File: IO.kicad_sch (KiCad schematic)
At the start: 0 parts

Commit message: First draft of USB and power module Plus some display started
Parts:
- added C1: 4.7uF, PCM_JLCPCB:C_0402, symbol PCM_JLCPCB-Capacitors:0402,4.7uF
- added C2: 100nF, PCM_JLCPCB:C_0603, symbol PCM_JLCPCB-Capacitors:0603,100nF
- added C3: 10uF, PCM_JLCPCB:C_0603, symbol PCM_JLCPCB-Capacitors:0603,10uF
- added IC1: TPS63001DRCR, TPS74901DRCR, symbol E-paper-library:TPS63001DRCR
- added J1: Connector, USB-TYPE-C-16P, PCM_JLCPCB:TYPE-C-SMD_HX-TYPE-C-16PIN, symbol PCM_JLCPCB-Extended:Connector, USB-TYPE-C-16P
- added L1: 2.2uH, symbol Device:L
- added R1, R2: 5.1kΩ, PCM_JLCPCB:R_0603, symbol PCM_JLCPCB-Resistors:0603,5.1kΩ
- added R3: 1MΩ, PCM_JLCPCB:R_0603, symbol PCM_JLCPCB-Resistors:0603,1MΩ
- added R4: 10Ω, PCM_JLCPCB:R_0603, symbol PCM_JLCPCB-Resistors:0603,10Ω
- added SW1: MK-12C02-G020, MK-12C02-G020_GSW, symbol E-paper-library:MK-12C02-G020
- added U1: SRV05-4.TCT, SO6_SOT23-6L, symbol E-paper-library:SRV05-4.TCT
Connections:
- new net: J1.B5 (CC2), R2.1
- new net: C1.1, J1.S1 (SHIELD), R3.1
- new net: J1.A5 (CC1), R1.2
- new net +3.3V: IC1.10 (FB)
- new net 5V_USB: C3.1, IC1.5 (VIN), J1.A9B4 (VBUS), J1.B9A4 (VBUS), R4.1, U1.5
- new net EN: IC1.6 (EN), SW1.3
- new net GNDD: C1.2, C2.2, C3.2, IC1.3 (PGND), IC1.9 (GND), IC1.EP1 (EP), J1.A12B1 (GND), J1.B12A1 (GND), R1.1, R2.2, R3.2, U1.2
- new net L1: IC1.4 (L1), L1.2
- new net L2: IC1.2 (L2), L1.1
- new net PS/SYNC: IC1.7 (PS/SYNC)
- new net USB D+: J1.A6 (D+), J1.B6 (D+), U1.1
- new net USB D-: J1.A7 (D-), J1.B7 (D-), U1.3
- new net VINA: C2.1, IC1.8 (VINA), R4.2, SW1.1
- no-connect marks 0 -> 5
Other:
- note added: "(Connection source)"
- note added: "Decoupling capacitor"
- note added: "ESD protection"
- note added: "Make sure C2 is close to TPS63001 GND!"
- note added: "Peripheral USB mode"
- note added: "Power module"
- note added: "Prevent EMI/ground loop"
- note added: "USB C module"
- note added: "USB Mode selection (audio, etc)"
- note added: "Voltage Regulator ON/OFF Switch"

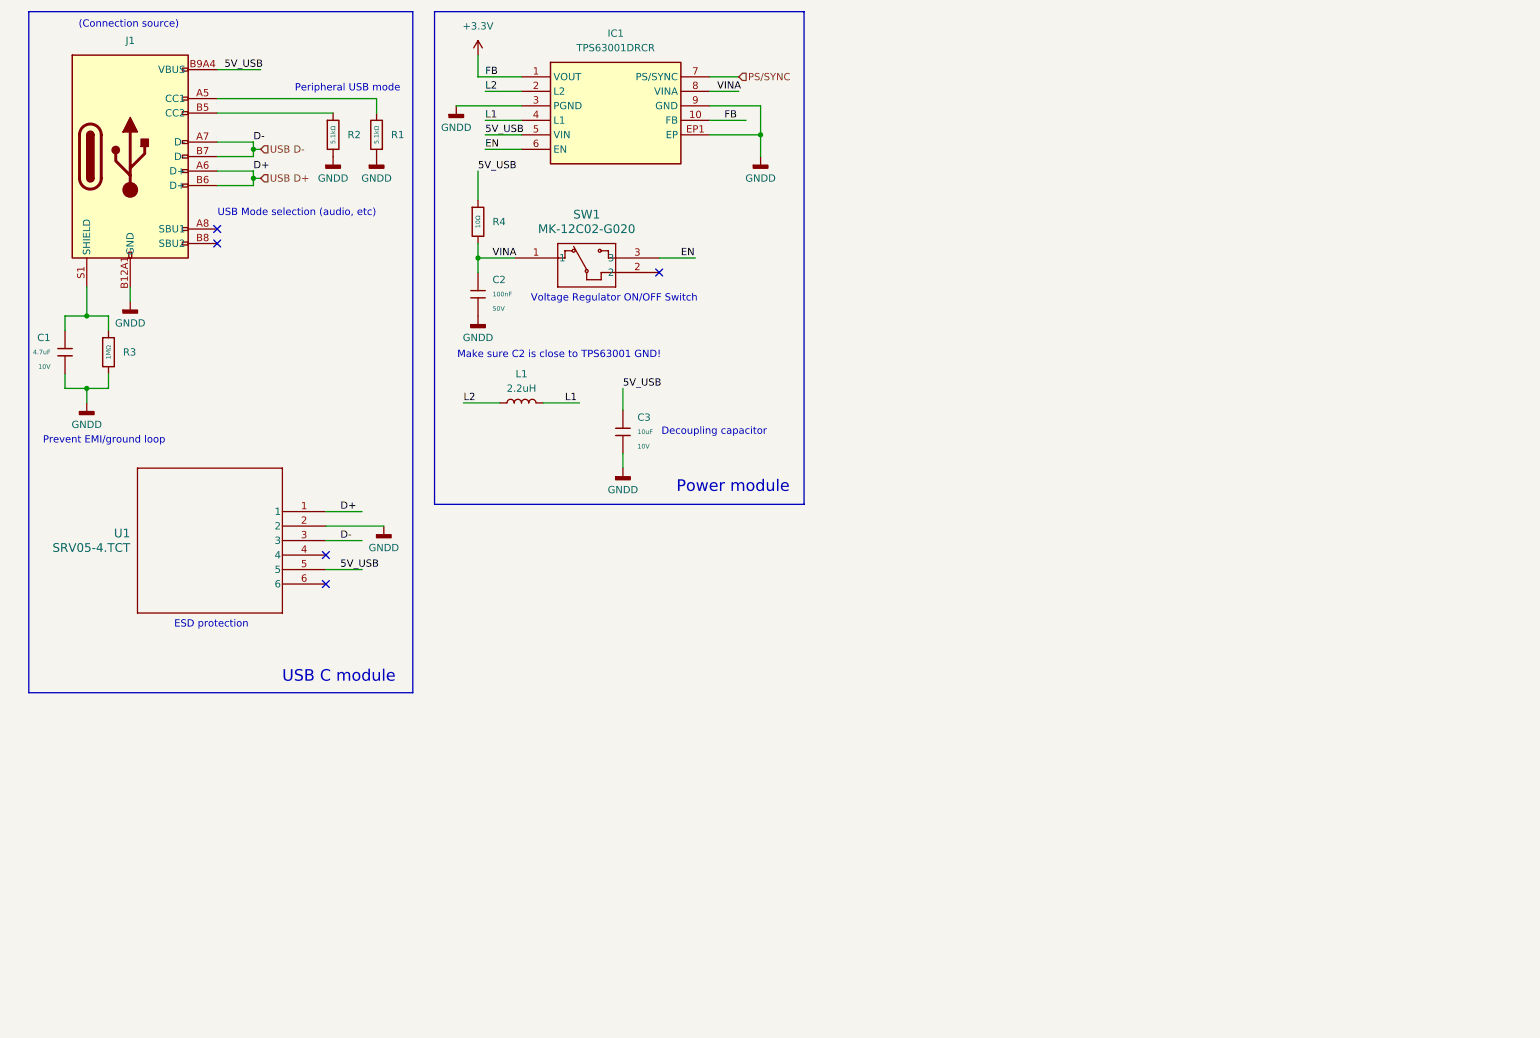
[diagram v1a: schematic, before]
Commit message: Only missing Eframe - Mostly finished MCU - Added Test points to IO - Added LiPo charger - Added Power Source Selection - Added SD card module + SPI connections
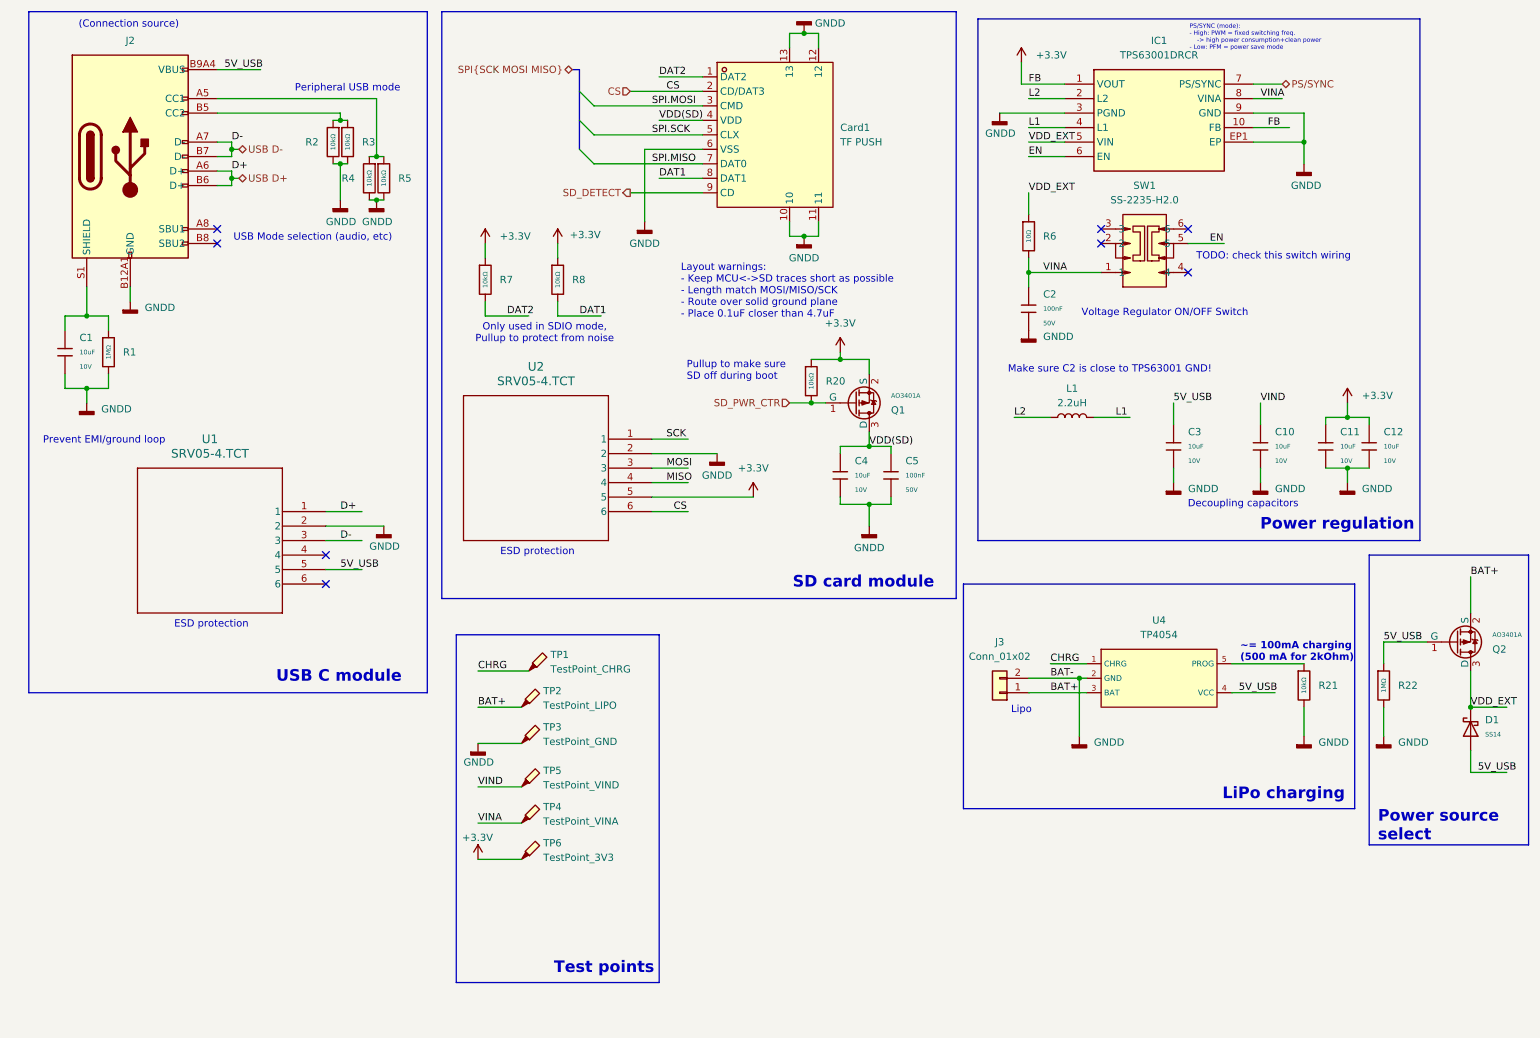
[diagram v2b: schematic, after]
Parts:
- removed C1: 4.7uF, PCM_JLCPCB:C_0402, symbol PCM_JLCPCB-Capacitors:0402,4.7uF
- removed R1, R2: 5.1kΩ, PCM_JLCPCB:R_0603, symbol PCM_JLCPCB-Resistors:0603,5.1kΩ
- removed SW1: MK-12C02-G020, MK-12C02-G020_GSW, symbol E-paper-library:MK-12C02-G020
- added C1, C10, C11, C12, C4: 10uF, PCM_JLCPCB:C_0603, symbol PCM_JLCPCB-Capacitors:0603,10uF
- added C5: 100nF, PCM_JLCPCB:C_0603, symbol PCM_JLCPCB-Capacitors:0603,100nF
- added Card1: TF PUSH, sd_card:TF-SMD_TF-PUSH, symbol E-paper-library:TFPUSH
- added D1: SS14, PCM_JLCPCB:D_SMA, symbol PCM_JLCPCB-Diodes:Schottky,SS14
- added J3: Conn_01x02, symbol Connector_Generic:Conn_01x02
- added Q1, Q2: AO3401A, PCM_JLCPCB:Q_SOT-23, symbol PCM_JLCPCB-Transistors:PMOS,AO3401A
- added R2, R20, R21, R3, R4, R5, R7, R8: 10kΩ, PCM_JLCPCB:R_0402, symbol PCM_JLCPCB-Resistors:0402,10kΩ
- added R22: 1MΩ, PCM_JLCPCB:R_0603, symbol PCM_JLCPCB-Resistors:0603,1MΩ
- added SW1: SS-2235-H2.0, switch:SW-TH_6P-L9.5-W3.5-P2.50_SS-2235-H2.0, symbol E-paper-library:SS-2235-H2.0
- added TP1: TestPoint_CHRG, symbol Connector:TestPoint_Probe
- added TP2: TestPoint_LIPO, symbol Connector:TestPoint_Probe
- added TP3: TestPoint_GND, symbol Connector:TestPoint_Probe
- added TP4: TestPoint_VINA, symbol Connector:TestPoint_Probe
- added TP5: TestPoint_VIND, symbol Connector:TestPoint_Probe
- added TP6: TestPoint_3V3, symbol Connector:TestPoint_Probe
- added U2: SRV05-4.TCT, SO6_SOT23-6L, symbol E-paper-library:SRV05-4.TCT
- added U4: TP4054, PCM_JLCPCB:SOT-23-5_L3.0-W1.7-P0.95-LS2.8-BL, symbol PCM_JLCPCB-Power:Battery, Li-Ion, 0.8A, TP4054
- renumbered J1 to J2, R3 to R1, R4 to R6
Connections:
- net +3.3V: now also C11.1, C12.1, Q1.2 (S), R20.1, R7.1, R8.1, TP6.1, U2.5
- net 5V_USB: now also D1.2, Q2.1 (G), R22.1, U4.4 (VCC); no longer IC1.5 (VIN), R6.1
- net EN: now also SW1.5
- net GNDD: now also C1.2, C10.2, C11.2, C12.2, C4.2, C5.2, Card1.10, Card1.11, Card1.12, Card1.13, Card1.6 (VSS), J3.2 (Pin_2), R2.2, R21.2, R22.2, R3.2, R4.2, R5.2, TP3.1, U2.2, U4.2 (GND)
- net VINA: now also SW1.1, TP4.1
- net at J2.B5 (CC2): now also R2.1, R3.1
- net at J2.S1 (SHIELD), R1.1: now also C1.1
- net at J2.A5 (CC1): now also R4.1, R5.1
- new net: R21.1, U4.5 (PROG)
- new net BAT+: J3.1 (Pin_1), Q2.2 (S), TP2.1, U4.3 (BAT)
- new net CHRG: TP1.1, U4.1 (CHRG)
- new net CS: Card1.2 (CD/DAT3), U2.6
- new net DAT1: Card1.8 (DAT1), R8.2
- new net DAT2: Card1.1 (DAT2), R7.2
- new net MISO: U2.4
- new net MOSI: U2.3
- new net SCK: U2.1
- new net SD_DETECT: Card1.9 (CD)
- new net SD_PWR_CTR: Q1.1 (G), R20.2
- new net SPI.MISO: Card1.7 (DAT0)
- new net SPI.MOSI: Card1.3 (CMD)
- new net SPI.SCK: Card1.5 (CLX)
- new net VDD(SD): C4.1, C5.1, Card1.4 (VDD), Q1.3 (D)
- new net VDD_EXT: D1.1, IC1.5 (VIN), Q2.3 (D), R6.1
- new net VIND: C10.1, TP5.1
- no-connect marks 5 -> 8
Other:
- note added: "Decoupling capacitors"
- note added: "Layout warnings: - Keep MCU<->SD traces short as possible - Length match MOSI/MISO/SCK - Route over solid ground plane - Place 0.1uF closer than 4.7uF"
- note added: "LiPo charging"
- note added: "Lipo"
- note added: "Only used in SDIO mode, Pullup to protect from noise"
- note added: "PS/SYNC (mode): - High: PWM = fixed switching freq. -> high power consumption+clean power - Low: PFM = power save mode"
- note added: "Power regulation"
- note added: "Power source select"
- note added: "Pullup to make sure SD off during boot"
- note added: "SD card module"
- note added: "TODO: check this switch wiring"
- note added: "Test points"
- note added: "~= 100mA charging (500 mA for 2kOhm)"
- note removed: "Decoupling capacitor"
- note removed: "Power module"
- moved on the sheet: C2, C3, IC1, L1, R6

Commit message: Added eframe circuit: - Must replace 10uF caps with higher voltage rated ones - Should double check all the wiring - Assign MCU GPIOs now that all peripherals have their pins assigned
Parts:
- removed L1: 2.2uH, symbol Device:L
- added L2: 2.2uH,50mA, PCM_JLCPCB:L_0805, symbol PCM_JLCPCB-Inductors:2.2uH,50mA
- added TP6: TestPoint_VIND, symbol Connector:TestPoint_Probe
- renumbered C1 to C12, C4 to C13, C5 to C14, C3 to C15, C2 to C16, C10 to C17, C11 to C18, C12 to C19, D1 to D4, J2 to J1, J3 to J2, Q1 to Q3, Q2 to Q4, R3 to R10, R4 to R11, R5 to R12, R7 to R13, R8 to R14, R20 to R15, R6 to R16, R21 to R17, R22 to R18, R1 to R8, R2 to R9, TP2 to TP1, TP3 to TP2, TP4 to TP3, TP6 to TP4, TP1 to TP7, U4 to U3
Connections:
- net EN: now also C16.1, IC1.8 (VINA), R16.2, TP3.1; no longer SW1.5
- net L1: now also L2.2
- net L2: now also L2.1
- net VDD_EXT: now also SW1.3, TP5.1; no longer D4.1, Q4.3 (D)
- net VIND: no longer TP5.1
- net SD_PWR_CTR renamed SD3V3_EN
- removed net VINA: C16.1, IC1.8 (VINA), R16.2, SW1.1, TP3.1
- new net VDD_EXT_OPEN: D4.1, Q4.3 (D), SW1.5, TP6.1
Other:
- note added: "Bulk capacitors"
- note added: "Electrical ON/OFF"
- note removed: "Decoupling capacitors"
- note removed: "TODO: check this switch wiring"
- moved on the sheet: C15, C17, C18, C19, D4, J2, Q4, R17, R18, TP3, TP4, TP5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

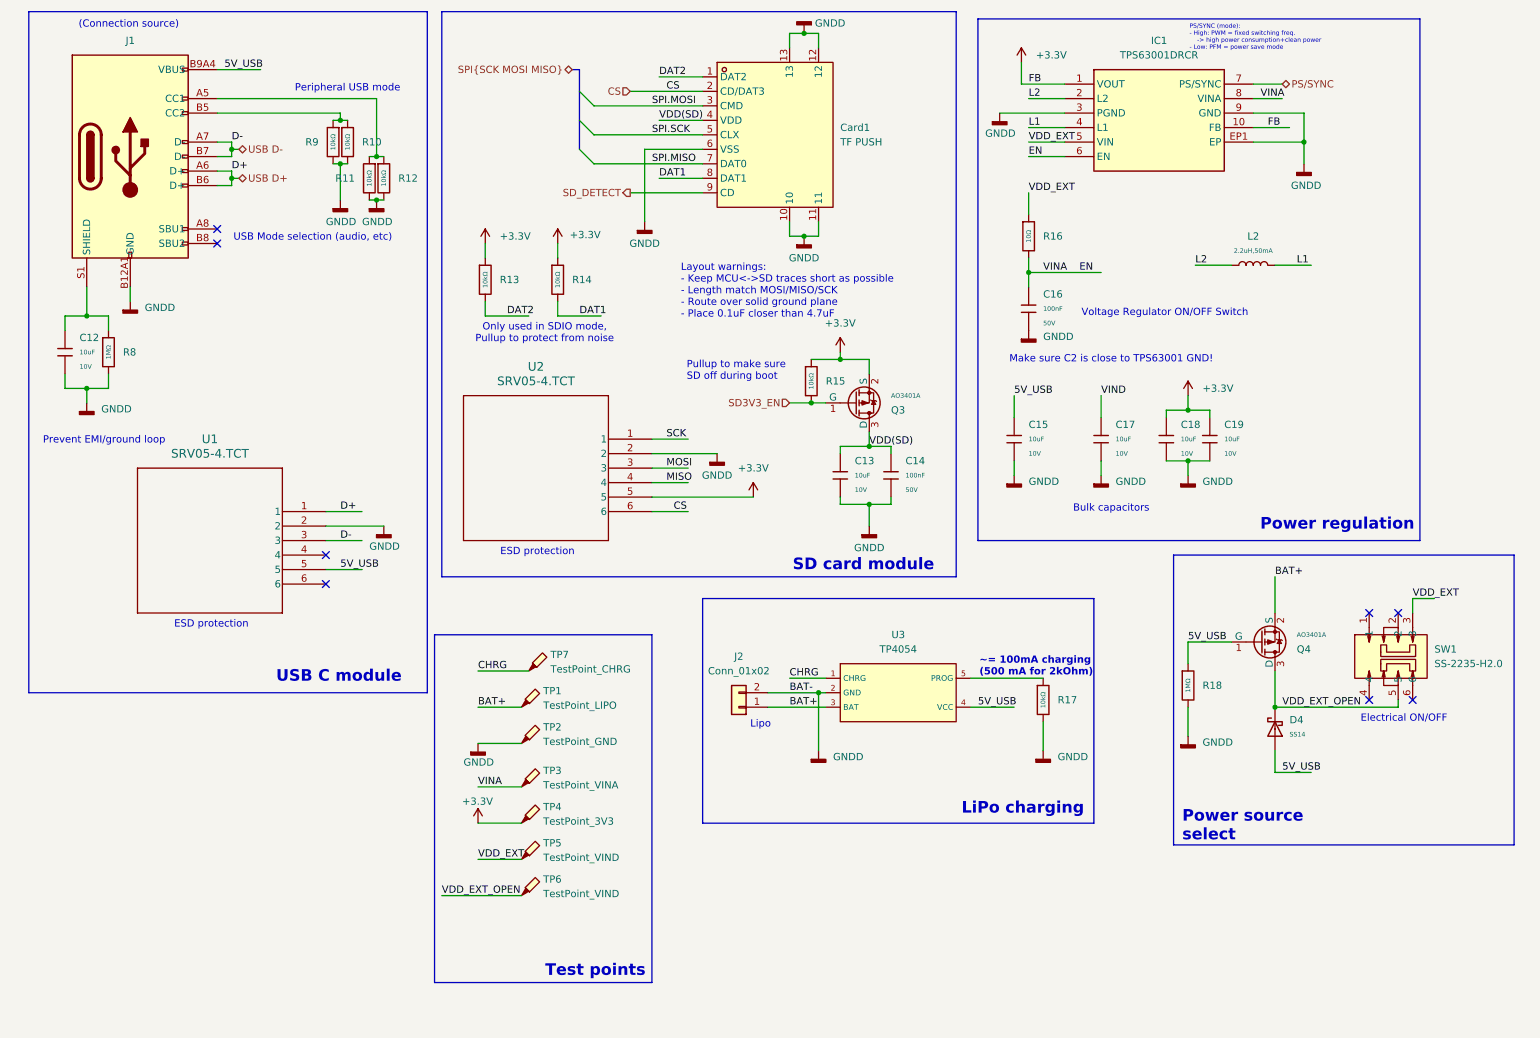
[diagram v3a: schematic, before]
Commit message: Final touches on schematic: Added test points Added LED Fixed symbol footprints
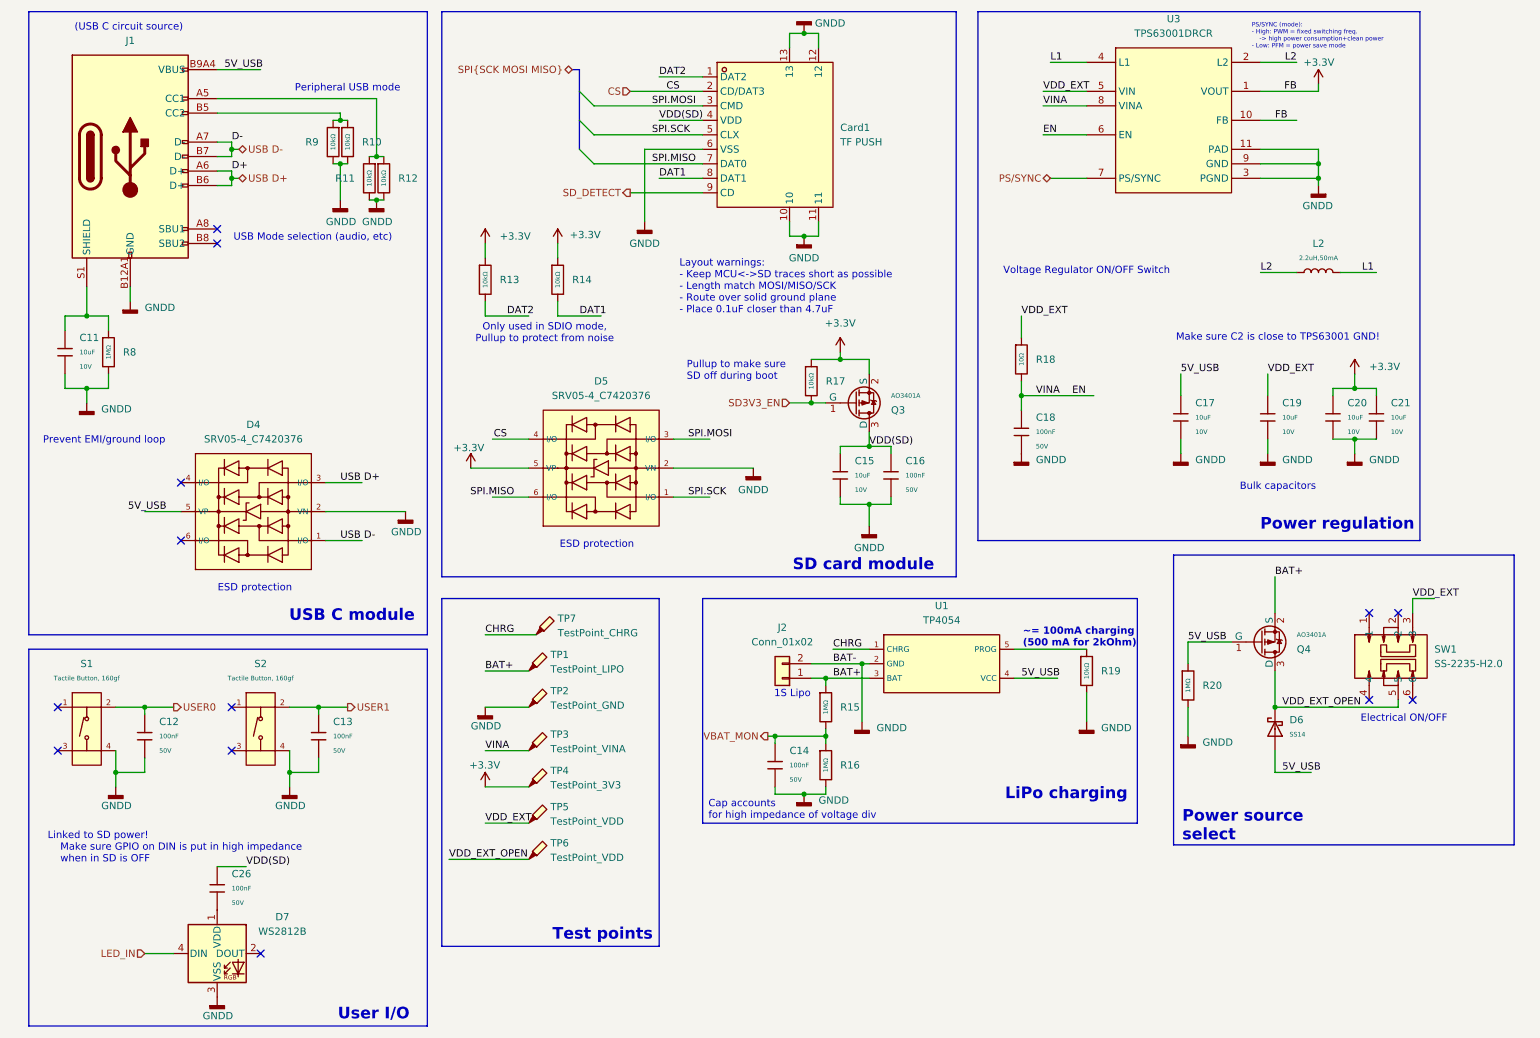
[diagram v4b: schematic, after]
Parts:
- removed IC1: TPS63001DRCR, TPS74901DRCR, symbol E-paper-library:TPS63001DRCR
- removed U1, U2: SRV05-4.TCT, SO6_SOT23-6L, symbol E-paper-library:SRV05-4.TCT
- added C12, C13, C14, C26: 100nF, PCM_JLCPCB:C_0603, symbol PCM_JLCPCB-Capacitors:0603,100nF
- added D4, D5: SRV05-4_C7420376, PCM_JLCPCB:SOT-23-6_L2.9-W1.6-P0.95-LS2.8-BL-1, symbol PCM_JLCPCB-Diode-Packages:Package, SRV05-4_C7420376
- added D7: WS2812B, PCM_JLCPCB:LED_WS2812B_PLCC4_5.0x5.0mm_P3.2mm, symbol PCM_JLCPCB-Extended:LED, WS2812B, 5050
- added R15, R16: 1MΩ, PCM_JLCPCB:R_0603, symbol PCM_JLCPCB-Resistors:0603,1MΩ
- added S1, S2: Tactile Button, 160gf, PCM_JLCPCB:SW-SMD_4P-L5.1-W5.1-P3.70-LS6.5-TL-2, symbol PCM_JLCPCB-Connectors_Buttons:Tactile Button, 160gf, 12V, 50mA, 5.1mm
- added U3: TPS63001DRCR, TPS63001DRCR:VSON-10_L3.0-W3.0-P0.50-TL-EP_TPS62410DRCR, symbol E-paper-library:TPS63001DRCR
- Card1: footprint sd_card:TF-SMD_TF-PUSH -> Libraries:TF-SMD_TF-PUSH
- J2: footprint (none) -> Connector_PinHeader_2.54mm:PinHeader_1x02_P2.54mm_Vertical
- SW1: footprint switch:SW-TH_6P-L9.5-W3.5-P2.50_SS-2235-H2.0 -> Libraries:SW-TH_6P-L9.0-W3.6-P2.50_SS-2235-H2.0
- TP1, TP4: footprint (none) -> TestPoint:TestPoint_Pad_1.5x1.5mm
- TP2, TP3, TP7: footprint (none) -> TestPoint:TestPoint_Pad_D1.5mm
- TP5, TP6: value TestPoint_VIND -> TestPoint_VDD; footprint (none) -> TestPoint:TestPoint_Pad_1.5x1.5mm
- renumbered C12 to C11, C13 to C15, C14 to C16, C15 to C17, C16 to C18, C17 to C19, C18 to C20, C19 to C21, D4 to D6, R15 to R17, R16 to R18, R17 to R19, R18 to R20, U3 to U1
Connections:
- net VIND is gone; now on net VDD_EXT: C19.1
- net +3.3V: now also D5.5 (VP), U3.10 (FB)
- net 5V_USB: now also D4.5 (VP)
- net BAT+: now also R15.1
- net CS: now also D5.4 (I/O)
- net EN: now also U3.6 (EN), U3.8 (VINA)
- net GNDD: now also C12.2, C13.2, C14.2, D4.2 (VN), D5.2 (VN), D7.3 (VSS), R16.2, S1.4 (D), S2.4 (D), U3.11 (PAD), U3.3 (PGND), U3.9 (GND)
- net L1: now also U3.4 (L1)
- net L2: now also U3.2 (L2)
- net PS/SYNC: now also U3.7 (PS/SYNC)
- net SPI.MISO: now also D5.6 (I/O)
- net SPI.MOSI: now also D5.3 (I/O)
- net SPI.SCK: now also D5.1 (I/O)
- net USB D+: now also D4.3 (I/O)
- net USB D-: now also D4.1 (I/O)
- net VDD(SD): now also C26.1
- net VDD_EXT: now also U3.5 (VIN)
- new net: C26.2, D7.1 (VDD)
- new net LED_IN: D7.4 (DIN)
- new net USER0: C12.1, S1.2 (B)
- new net USER1: C13.1, S2.2 (B)
- new net VBAT_MON: C14.1, R15.2, R16.1
- no-connect marks 8 -> 13
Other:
- note added: "(USB C circuit source)"
- note added: "1S Lipo"
- note added: "Cap accounts for high impedance of voltage div"
- note added: "Linked to SD power! Make sure GPIO on DIN is put in high impedance when in SD is OFF"
- note added: "User I/O"
- note removed: "(Connection source)"
- note removed: "Lipo"
- moved on the sheet: C17, C18, C19, C20, C21, J2, L2, R18, R19, TP1, TP2, TP3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
